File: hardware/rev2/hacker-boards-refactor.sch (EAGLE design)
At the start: 38 parts, among them J1 MICRO_USB_B_JST_MC5BR3-M404-4S

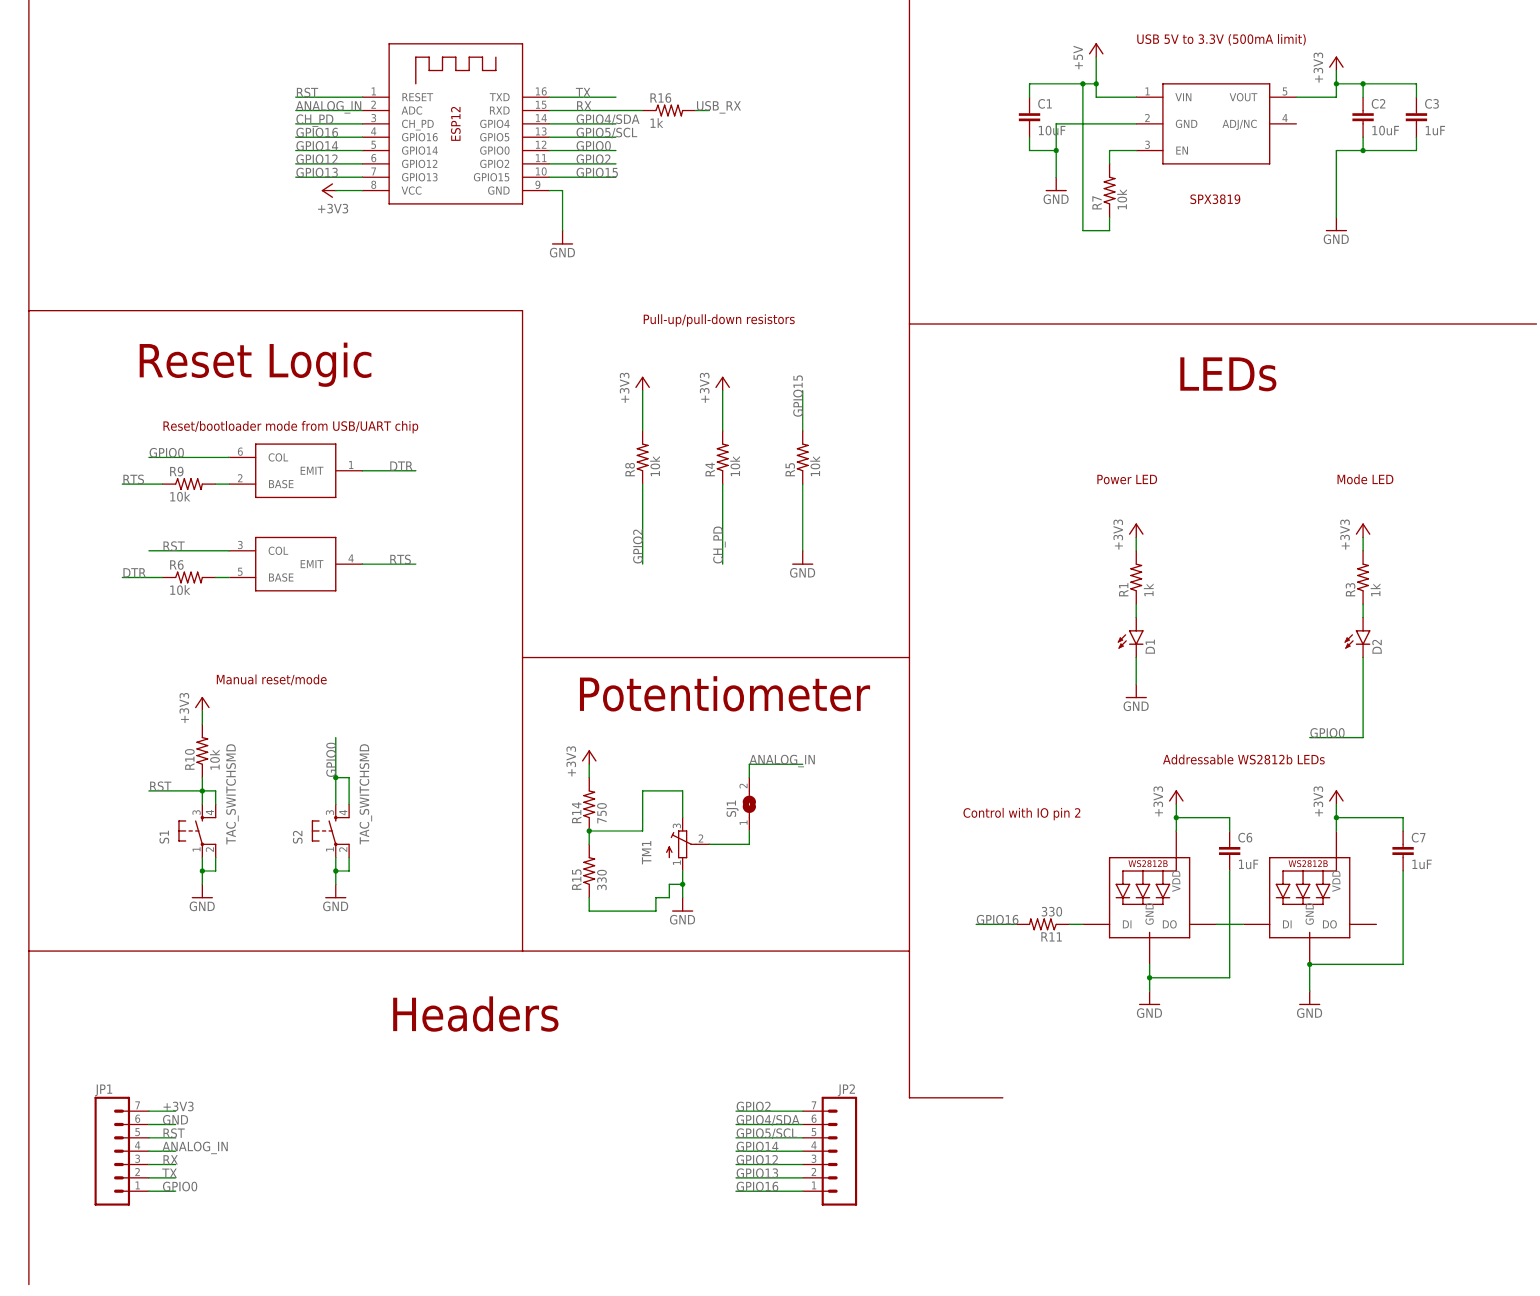
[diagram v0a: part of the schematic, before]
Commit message: Shrank the board and re-placed components, looking for an optimized second prototyping run
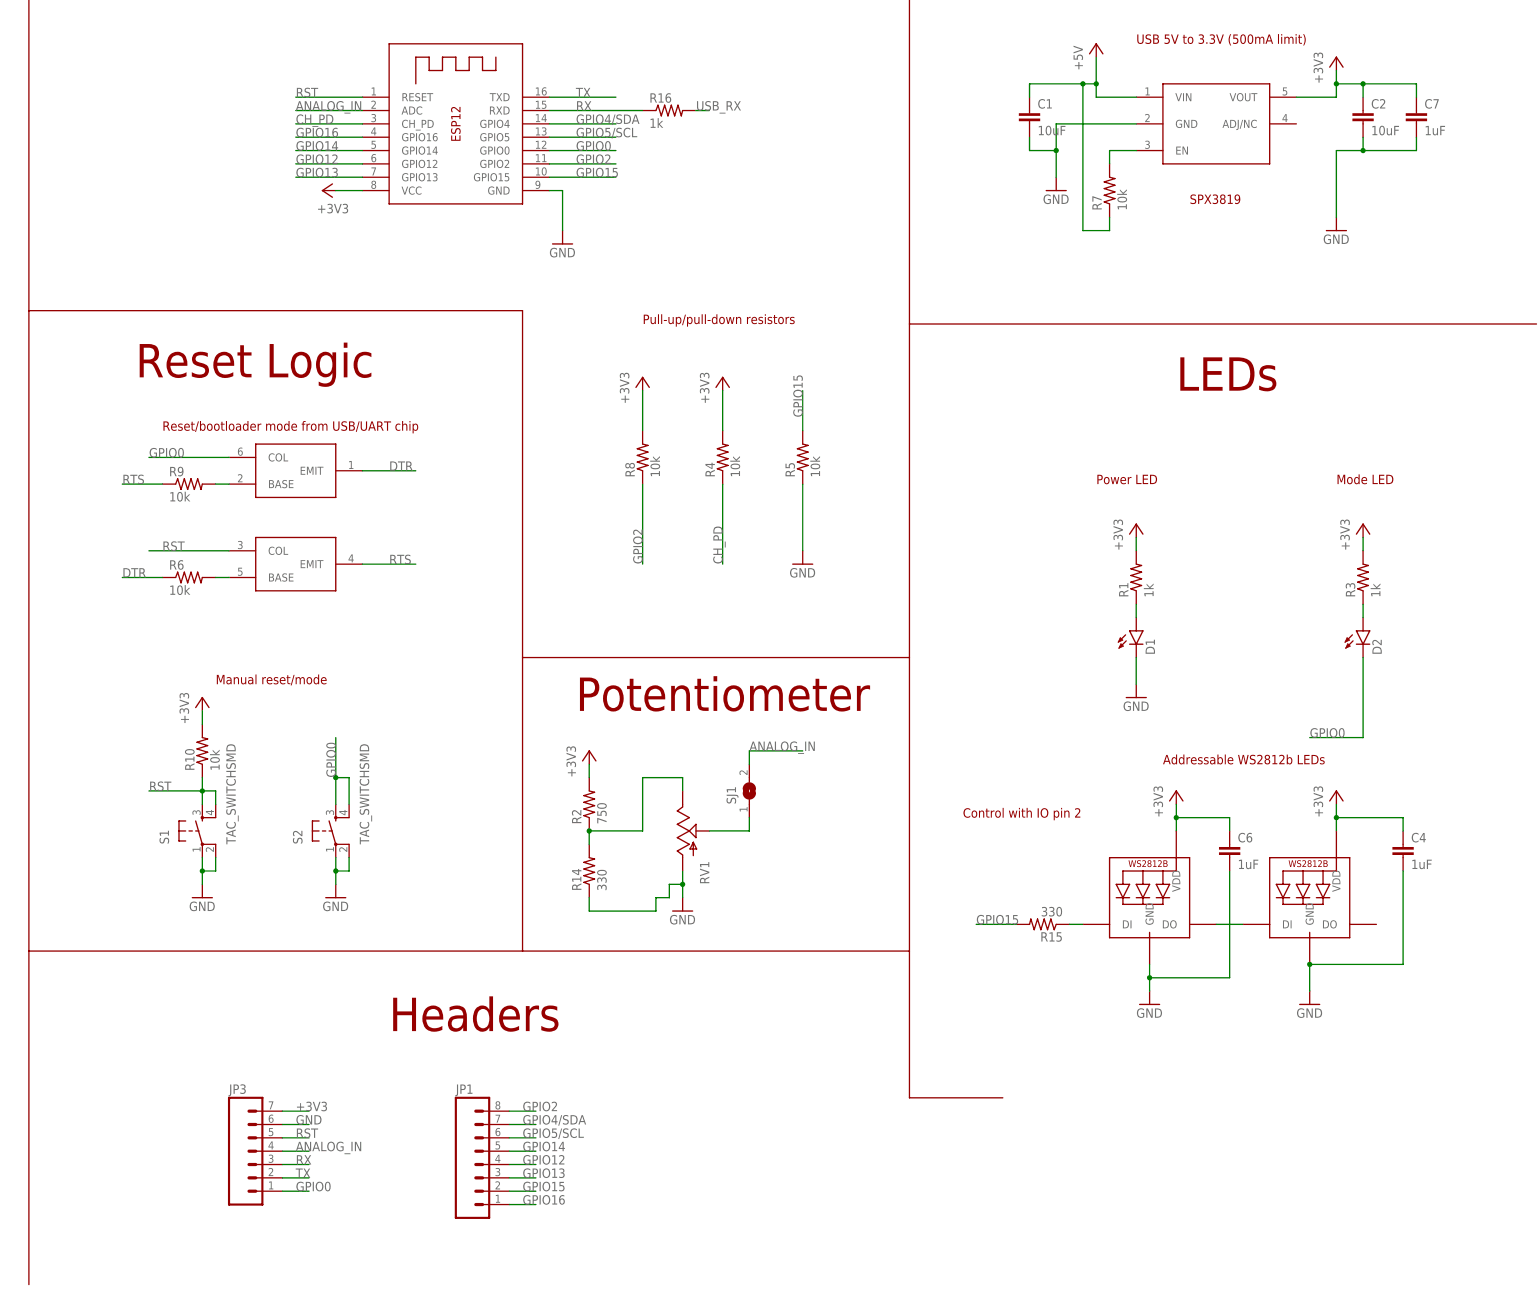
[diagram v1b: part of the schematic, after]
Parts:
- removed C3: 1uF, hacker-board:C0805
- removed JP2: (no value), hacker-board:M07LONGPADS
- removed R11: 330, resistor:R-US_R0805
- removed TM1: (no value), adafruit:TRIMPOTTC33X
- added C4: 1uF, resistor:C-EUC0402
- added JP3: (no value), SparkFun-Connectors:M07
- added R2: 750, resistor:R-US_R0402
- added RV1: (no value), SparkFun-Electromechanical:POTALPS-KIT
- C6, C7: device hacker-board:C0805 -> resistor:C-EUC0402
- JP1: device hacker-board:M07LONGPADS -> SparkFun-Connectors:M08
- R1, R15, R3: device resistor:R-US_R0805 -> resistor:R-US_R0402
- R14: value 750 -> 330; device resistor:R-US_R0805 -> resistor:R-US_R0402
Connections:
- net +3V3: now also C4.1, JP3.7, R2.2; no longer C3.1, JP1.7, R14.2
- net ANALOG_IN: now also JP3.4; no longer JP1.4
- net GND: now also C4.2, JP3.6, R14.1, RV1.A; no longer C3.2, JP1.6, R15.1, TM1.A
- net GPIO0: now also JP3.1; no longer JP1.1
- net GPIO12: now also JP1.4; no longer JP2.3
- net GPIO13: now also JP1.3; no longer JP2.2
- net GPIO14: now also JP1.5; no longer JP2.4
- net GPIO15: now also JP1.2, R15.2
- net GPIO16: now also JP1.1; no longer JP2.1, R11.2
- net GPIO2: now also JP1.8; no longer JP2.7
- net GPIO4/SDA: now also JP1.7; no longer JP2.6
- net GPIO5/SCL: now also JP1.6; no longer JP2.5
- net N$12: now also RV1.S; no longer TM1.S
- net N$4: now also R14.2, R2.1, RV1.E; no longer R14.1, R15.2, TM1.E
- net N$6: now also R15.1; no longer R11.1
- net RST: now also JP3.5; no longer JP1.5
- net RX: now also JP3.3; no longer JP1.3
- net TX: now also JP3.2; no longer JP1.2
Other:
- moved on the sheet: C7, R14, R15, SJ1

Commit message: Removed fuse, played around/shrunk board dimensions some more
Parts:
- removed U$1: USB-FUSE, hacker-board:USB-FUSE
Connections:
- removed net N$2: J1.+5V, U$1.IN
- net +5V: now also J1.+5V; no longer U$1.OUT
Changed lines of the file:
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@@
 <part name="GND6" library="supply1" deviceset="GND" device=""/>
 <part name="+3V5" library="supply1" deviceset="+3V3" device=""/>
-<part name="U$1" library="hacker-board" deviceset="USB-FUSE" device=""/>
 <part name="J1" library="hacker-board" deviceset="MICRO_USB_B_JST_MC5BR3-M404-4S" device=""/>
 <part name="D1" library="hacker-board" deviceset="LED" device="0603"/>
@@
 <instance part="GND6" gate="1" x="40.64" y="-17.78"/>
 <instance part="+3V5" gate="G$1" x="261.62" y="53.34"/>
-<instance part="U$1" gate="G$1" x="-25.4" y="114.3"/>
 <instance part="J1" gate="G$1" x="-50.8" y="127" rot="R180"/>
 <instance part="D1" gate="G$1" x="218.44" y="33.02"/>
@@
 </segment>
 <segment>
-<pinref part="U$1" gate="G$1" pin="OUT"/>
-<wire x1="-10.16" y1="114.3" x2="-5.08" y2="114.3" width="0.1524" layer="91"/>
 <pinref part="P+1" gate="1" pin="+5V"/>
 <wire x1="-5.08" y1="114.3" x2="-5.08" y2="119.38" width="0.1524" layer="91"/>
@@
 <junction x="-5.08" y="114.3"/>
 <pinref part="C8" gate="G$1" pin="1"/>
+<pinref part="J1" gate="G$1" pin="+5V"/>
+<wire x1="-43.18" y1="121.92" x2="-40.64" y2="121.92" width="0.1524" layer="91"/>
+<wire x1="-40.64" y1="121.92" x2="-40.64" y2="114.3" width="0.1524" layer="91"/>
+<wire x1="-40.64" y1="114.3" x2="-5.08" y2="114.3" width="0.1524" layer="91"/>
 </segment>
 <segment>
@@
 </segment>
 </net>
-<net name="N$2" class="0">
-<segment>
-<pinref part="J1" gate="G$1" pin="+5V"/>
-<wire x1="-43.18" y1="121.92" x2="-40.64" y2="121.92" width="0.1524" layer="91"/>
-<pinref part="U$1" gate="G$1" pin="IN"/>
-<wire x1="-40.64" y1="121.92" x2="-40.64" y2="114.3" width="0.1524" layer="91"/>
-</segment>
-</net>

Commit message: Added huge solder stop area in the MHacks Refactor logo form
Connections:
- net GPIO12: now also JP1.5; no longer JP1.4
- net GPIO13: now also JP1.4; no longer JP1.3
- net GPIO14: now also JP1.3; no longer JP1.5
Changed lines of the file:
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@@
 <?xml version="1.0" encoding="utf-8"?>
 <!DOCTYPE eagle SYSTEM "eagle.dtd">
-<eagle version="7.5.0">
+<eagle version="7.3.0">
 <drawing>
 <settings>
@@
 </segment>
 <segment>
+<pinref part="JP1" gate="G$1" pin="3"/>
+<wire x1="99.06" y1="-71.12" x2="104.14" y2="-71.12" width="0.1524" layer="91"/>
+<label x="101.6" y="-71.12" size="1.778" layer="95"/>
+</segment>
+</net>
+<net name="GPIO12" class="0">
+<segment>
+<pinref part="X1" gate="G$1" pin="GPIO12"/>
+<wire x1="71.12" y1="121.92" x2="58.42" y2="121.92" width="0.1524" layer="91"/>
+<label x="58.42" y="121.92" size="1.778" layer="95"/>
+</segment>
+<segment>
 <pinref part="JP1" gate="G$1" pin="5"/>
 <wire x1="99.06" y1="-66.04" x2="104.14" y2="-66.04" width="0.1524" layer="91"/>
@@
 </segment>
 </net>
-<net name="GPIO12" class="0">
-<segment>
-<pinref part="X1" gate="G$1" pin="GPIO12"/>
-<wire x1="71.12" y1="121.92" x2="58.42" y2="121.92" width="0.1524" layer="91"/>
-<label x="58.42" y="121.92" size="1.778" layer="95"/>
+<net name="GPIO13" class="0">
+<segment>
+<pinref part="X1" gate="G$1" pin="GPIO13"/>
+<wire x1="71.12" y1="119.38" x2="58.42" y2="119.38" width="0.1524" layer="91"/>
+<label x="58.42" y="119.38" size="1.778" layer="95"/>
 </segment>
 <segment>
@@
 </segment>
 </net>
-<net name="GPIO13" class="0">
-<segment>
-<pinref part="X1" gate="G$1" pin="GPIO13"/>
-<wire x1="71.12" y1="119.38" x2="58.42" y2="119.38" width="0.1524" layer="91"/>
-<label x="58.42" y="119.38" size="1.778" layer="95"/>
-</segment>
-<segment>
-<pinref part="JP1" gate="G$1" pin="3"/>
-<wire x1="99.06" y1="-71.12" x2="104.14" y2="-71.12" width="0.1524" layer="91"/>
-<label x="101.6" y="-71.12" size="1.778" layer="95"/>
-</segment>
-</net>
